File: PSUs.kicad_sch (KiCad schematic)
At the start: 33 parts, among them J19 Barrel_Jack, J20 AMP171826-4, Q1 DMP3013SFV-7, U16 AP64501SP-13

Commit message: removed HDMI, CAM and DISP1 connectors
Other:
- company: © 2020-2022 Raspberry Pi Ltd (formerly Raspberry Pi (Trading) Ltd.) -> (none)
- title: Compute Module 4 IO Board - PSUs -> Bitcart
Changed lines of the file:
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@@
   (paper "A4")
   (title_block
-    (title "Compute Module 4 IO Board - PSUs")
-    (company "© 2020-2022 Raspberry Pi Ltd (formerly Raspberry Pi (Trading) Ltd.)")
-    (comment 1 "www.raspberrypi.com")
+    (title "Bitcart")
+    (date "2023-09-15")
+    (rev "1")
   )
   (junction (at 76.2 130.302) (diameter 1.016) (color 0 0 0 0)

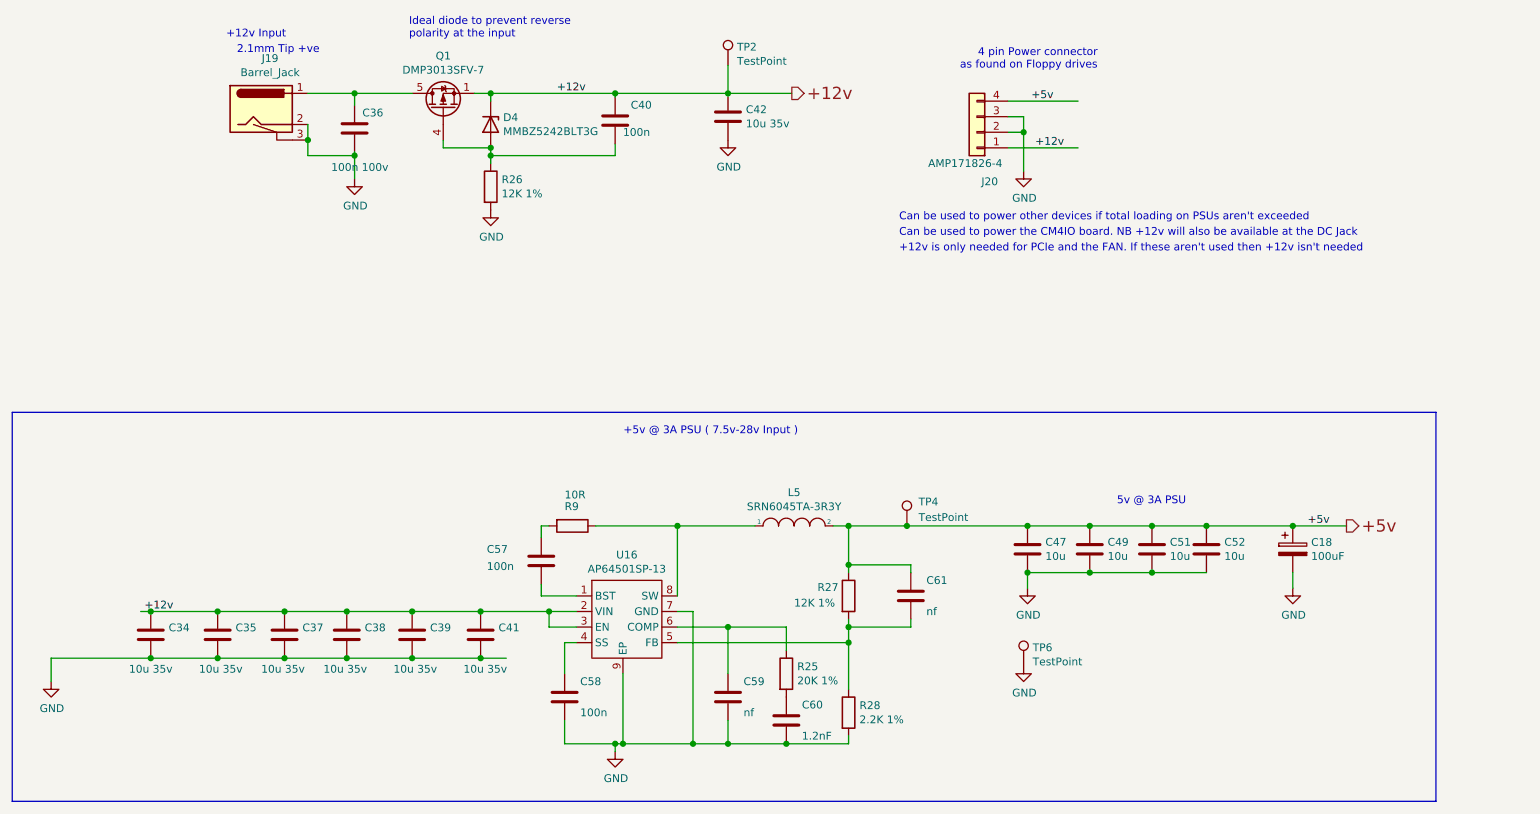
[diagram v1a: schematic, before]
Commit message: added hashboard connectors. added GPU power connector
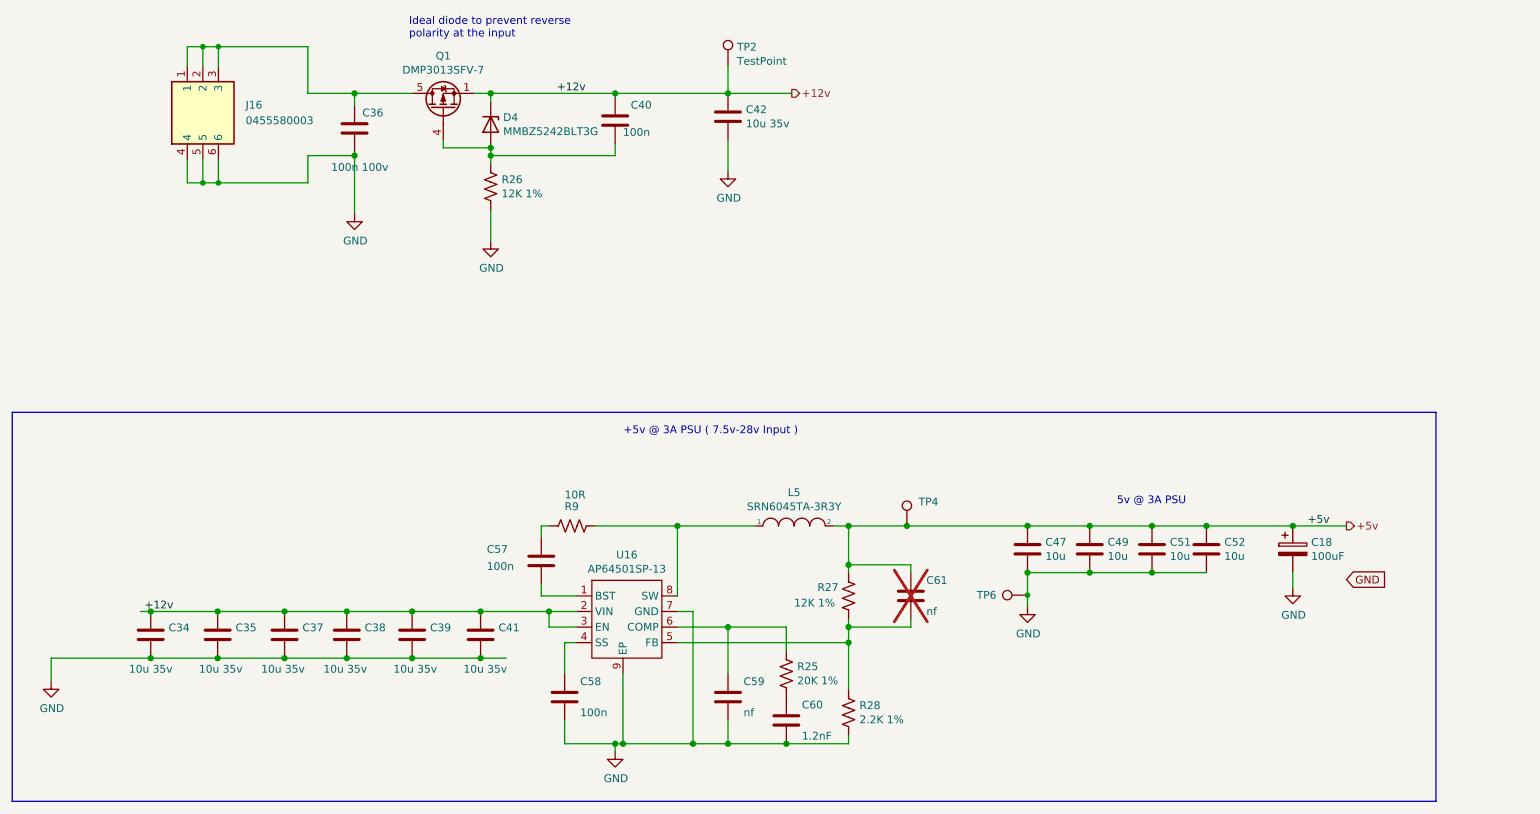
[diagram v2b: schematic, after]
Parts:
- removed J19: Barrel_Jack, CM4IO:BarrelJack_Horizontal, symbol CM4IO:Barrel_Jack
- removed J20: AMP171826-4, 171826-4:TE_171826-4, symbol Connector_Generic:Conn_01x04
- added J16: 0455580003, bitcart:0455580003, symbol bitcart:0455580003
- C61: now not fitted
- R25, R26, R27, R28, R9: symbol Device:R -> Device:R_US
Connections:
- net GND: now also J16.4, J16.5, J16.6
- net at C36.1, Q1.5 (D): now also J16.1, J16.2, J16.3
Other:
- note removed: "+12v Input"
- note removed: "+12v is only needed for PCIe and the FAN. If these aren't used then +12v isn't needed"
- note removed: "2.1mm Tip +ve"
- note removed: "4 pin Power connector as found on Floppy drives"
- note removed: "Can be used to power other devices if total loading on PSUs aren't exceeded"
- note removed: "Can be used to power the CM4IO board. NB +12v will also be available at the DC Jack"
- moved on the sheet: TP6

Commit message: extended the board to make room for IO connectors. added the vertical display connector.
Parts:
- TP2, TP4, TP6: footprint TestPoint:TestPoint_Pad_2.0x2.0mm -> TestPoint:TestPoint_Pad_D1.5mm
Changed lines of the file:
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@@
       (effects (font (size 1.27 1.27)) (justify left))
     )
-    (property "Footprint" "TestPoint:TestPoint_Pad_2.0x2.0mm" (at 153.67 41.148 0)
+    (property "Footprint" "TestPoint:TestPoint_Pad_D1.5mm" (at 153.67 41.148 0)
       (effects (font (size 1.27 1.27)) hide)
     )
@@
       (effects (font (size 1.27 1.27)) (justify left) hide)
     )
-    (property "Footprint" "TestPoint:TestPoint_Pad_2.0x2.0mm" (at 197.485 122.555 0)
+    (property "Footprint" "TestPoint:TestPoint_Pad_D1.5mm" (at 197.485 122.555 0)
       (effects (font (size 1.27 1.27)) hide)
     )
@@
       (effects (font (size 1.27 1.27)) (justify left) hide)
     )
-    (property "Footprint" "TestPoint:TestPoint_Pad_2.0x2.0mm" (at 182.88 116.332 0)
-      (effects (font (size 1.27 1.27)) hide)
-    )
+    (property "Footprint" "TestPoint:TestPoint_Pad_D1.5mm" (at 182.88 116.332 0)
+      (effects (font (size 1.27 1.27)) hide)
+    )

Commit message: added a lot more parts
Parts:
- C40, C57, C58: value 100n -> 0.1uF; DK (none) -> 478-KGM05AR71C104KHCT-ND; PARTNO (none) -> KGM05AR71C104KH; Part Description 0.1uF 10% 16V Ceramic Capacitor X7R 0402 (1005 Metric) -> (none)
- D4: DK (none) -> MMBZ5242BLT3GOSCT-ND; Field4 Digikey -> (none); Field5 MMBZ5242BLT3GOSCT-ND -> (none); Field6 MMBZ5242BLT3G -> (none); Field7 Onsemi -> (none); PARTNO (none) -> MMBZ5242BLT3G; Part Description Zener Diode 12V 225mW 5% Surface Mount SOT-23-3 (TO-236) -> (none)
- L5: DK (none) -> SRN6045TA-3R3YCT-ND; Field4 Farnell -> (none); Field5 2616889 -> (none); Field7 Bourns -> (none); Part Description 3.3µH Semi-Shielded Wirewound Inductor 7.8A 21mOhm Nonstand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 -> (none)
- Q1: DK (none) -> DMP3013SFV-7DICT-ND; Field4 Farnell -> (none); Field5 3405192 -> (none); Field6 DMP3013SFV-7 -> (none); Field7 Diodes -> (none); PARTNO (none) -> DMP3013SFV-7; Part Description DMP3013SFV-7 - Power MOSFET, P Channel, 30 V, 12 A, 0.008 o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 -> (none)
- U16: DK (none) -> 31-AP64501SP-13CT-ND; Field4 Digikey -> (none); Field5 31-AP64501SP-13CT-ND -> (none); Field6 AP64501SP-13 -> (none); Field7 Diodes -> (none); PARTNO (none) -> AP64501SP-13; Part Description Buck Switching Regulator IC Positive Adjustable 0.8V 1 Outp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 -> (none)
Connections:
- net +12v: now also D4.3 (K); no longer D4.1 (K)
- net at C40.2, Q1.4 (G), R26.1: now also D4.1 (A); no longer D4.2 (A)
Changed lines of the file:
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@@
       (effects (font (size 1.27 1.27)) hide)
     )
-    (property "Field4" "Digikey" (at 109.855 50.8 0)
-      (effects (font (size 1.27 1.27)) hide)
-    )
-    (property "Field5" "	MMBZ5242BLT3GOSCT-ND" (at 109.855 50.8 0)
-      (effects (font (size 1.27 1.27)) hide)
-    )
-    (property "Field6" "MMBZ5242BLT3G" (at 109.855 50.8 0)
-      (effects (font (size 1.27 1.27)) hide)
-    )
-    (property "Field7" "Onsemi" (at 109.855 50.8 0)
-      (effects (font (size 1.27 1.27)) hide)
-    )
-    (property "Part Description" "	Zener Diode 12V 225mW 5% Surface Mount SOT-23-3 (TO-236)" (at 109.855 50.8 0)
-      (effects (font (size 1.27 1.27)) hide)
-    )
-    (pin "1")
-    (pin "2")
+    (property "DK" "MMBZ5242BLT3GOSCT-ND" (at 109.855 50.8 0)
+      (effects (font (size 1.27 1.27)) hide)
+    )
+    (property "PARTNO" "MMBZ5242BLT3G" (at 109.855 50.8 0)
+      (effects (font (size 1.27 1.27)) hide)
+    )
+    (pin "1")
+    (pin "2")
+    (pin "3")
     (instances
       (project "bitcart"
@@
       (effects (font (size 1.27 1.27)) (justify left))
     )
-    (property "Value" "100n" (at 131.445 52.07 0)
+    (property "Value" "0.1uF" (at 131.445 52.07 0)
       (effects (font (size 1.27 1.27)) (justify left))
     )
@@
       (effects (font (size 1.27 1.27)) hide)
     )
-    (property "Part Description" "	0.1uF 10% 16V Ceramic Capacitor X7R 0402 (1005 Metric)" (at 130.175 50.165 0)
+    (property "Part Description" "" (at 130.175 50.165 0)
       (effects (font (size 1.27 1.27)) hide)
     )
@@
       (effects (font (size 1.27 1.27)) hide)
     )
+    (property "DK" "478-KGM05AR71C104KHCT-ND" (at 130.175 50.165 0)
+      (effects (font (size 1.27 1.27)) hide)
+    )
+    (property "PARTNO" "KGM05AR71C104KH" (at 130.175 50.165 0)
+      (effects (font (size 1.27 1.27)) hide)
+    )
     (pin "1")
     (pin "2")
@@
       (effects (font (size 1.27 1.27)) (justify left))
     )
-    (property "Value" "100n" (at 109.22 122.936 0)
+    (property "Value" "0.1uF" (at 109.22 122.936 0)
       (effects (font (size 1.27 1.27)) (justify left))
     )
@@
       (effects (font (size 1.27 1.27)) hide)
     )
-    (property "Part Description" "	0.1uF 10% 16V Ceramic Capacitor X7R 0402 (1005 Metric)" (at 118.11 122.047 0)
+    (property "Part Description" "" (at 118.11 122.047 0)
       (effects (font (size 1.27 1.27)) hide)
     )
     (property "Field8" "110091611" (at 118.11 122.047 0)
+      (effects (font (size 1.27 1.27)) hide)
+    )
+    (property "DK" "478-KGM05AR71C104KHCT-ND" (at 118.11 122.047 0)
+      (effects (font (size 1.27 1.27)) hide)
+    )
+    (property "PARTNO" "KGM05AR71C104KH" (at 118.11 122.047 0)
       (effects (font (size 1.27 1.27)) hide)
     )
@@
       (effects (font (size 1.27 1.27)) hide)
     )
-    (property "Field4" "Farnell" (at 159.385 116.332 0)
-      (effects (font (size 1.27 1.27)) hide)
-    )
-    (property "Field5" "2616889" (at 159.385 116.332 0)
+    (property "DK" "SRN6045TA-3R3YCT-ND" (at 159.385 116.332 0)
       (effects (font (size 1.27 1.27)) hide)
     )
@@
       (effects (font (size 1.27 1.27)) hide)
     )
-    (property "Field7" "Bourns" (at 159.385 116.332 0)
-      (effects (font (size 1.27 1.27)) hide)
-    )
-    (property "Part Description" "3.3µH Semi-Shielded Wirewound Inductor 7.8A 21mOhm Nonstandard" (at 159.385 116.332 0)
-      (effects (font (size 1.27 1.27)) hide)
-    )
     (pin "1")
     (pin "2")
@@
       (effects (font (size 1.27 1.27)) hide)
     )
-    (property "Field4" "Digikey" (at 131.445 130.302 0)
-      (effects (font (size 1.27 1.27)) hide)
-    )
-    (property "Field5" "31-AP64501SP-13CT-ND" (at 131.445 130.302 0)
-      (effects (font (size 1.27 1.27)) hide)
-    )
-    (property "Field6" "AP64501SP-13" (at 131.445 130.302 0)
-      (effects (font (size 1.27 1.27)) hide)
-    )
-    (property "Field7" "Diodes" (at 131.445 130.302 0)
-      (effects (font (size 1.27 1.27)) hide)
-    )
-    (property "Part Description" "Buck Switching Regulator IC Positive Adjustable 0.8V 1 Output 5A 8-SOIC (0.154\", 3.90mm Width) Exposed Pad" (at 131.445 130.302 0)
+    (property "DK" "31-AP64501SP-13CT-ND" (at 131.445 130.302 0)
+      (effects (font (size 1.27 1.27)) hide)
+    )
+    (property "PARTNO" "AP64501SP-13" (at 131.445 130.302 0)
       (effects (font (size 1.27 1.27)) hide)
     )
@@
       (effects (font (size 1.27 1.27)) (justify left))
     )
-    (property "Value" "100n" (at 124.46 146.812 0)
+    (property "Value" "0.1uF" (at 124.46 146.812 0)
       (effects (font (size 1.27 1.27)) (justify left))
     )
@@
       (effects (font (size 1.27 1.27)) hide)
     )
-    (property "Part Description" "	0.1uF 10% 16V Ceramic Capacitor X7R 0402 (1005 Metric)" (at 121.92 144.272 0)
+    (property "Part Description" "" (at 121.92 144.272 0)
       (effects (font (size 1.27 1.27)) hide)
     )
     (property "Field8" "110091611" (at 121.92 144.272 0)
+      (effects (font (size 1.27 1.27)) hide)
+    )
+    (property "DK" "478-KGM05AR71C104KHCT-ND" (at 121.92 144.272 0)
+      (effects (font (size 1.27 1.27)) hide)
+    )
+    (property "PARTNO" "KGM05AR71C104KH" (at 121.92 144.272 0)
       (effects (font (size 1.27 1.27)) hide)
     )
@@
       (effects (font (size 1.27 1.27)) (justify left) hide)
     )
-    (property "Field4" "Farnell" (at 102.108 48.26 0)
-      (effects (font (size 1.27 1.27)) hide)
-    )
-    (property "Field5" "3405192" (at 102.108 48.26 0)
-      (effects (font (size 1.27 1.27)) hide)
-    )
-    (property "Field6" "DMP3013SFV-7" (at 102.108 48.26 0)
-      (effects (font (size 1.27 1.27)) hide)
-    )
-    (property "Field7" "Diodes" (at 102.108 48.26 0)
-      (effects (font (size 1.27 1.27)) hide)
-    )
-    (property "Part Description" "DMP3013SFV-7 -  Power MOSFET, P Channel, 30 V, 12 A, 0.008 ohm, PowerDI3333, Surface Mount" (at 102.108 48.26 0)
-      (effects (font (size 1.27 1.27)) hide)
-    )
+    (property "DK" "DMP3013SFV-7DICT-ND" (at 102.108 48.26 90)
+      (effects (font (size 1.27 1.27)) hide)
+    )
+    (property "PARTNO" "DMP3013SFV-7" (at 102.108 48.26 90)
+      (effects (font (size 1.27 1.27)) hide)
+    )

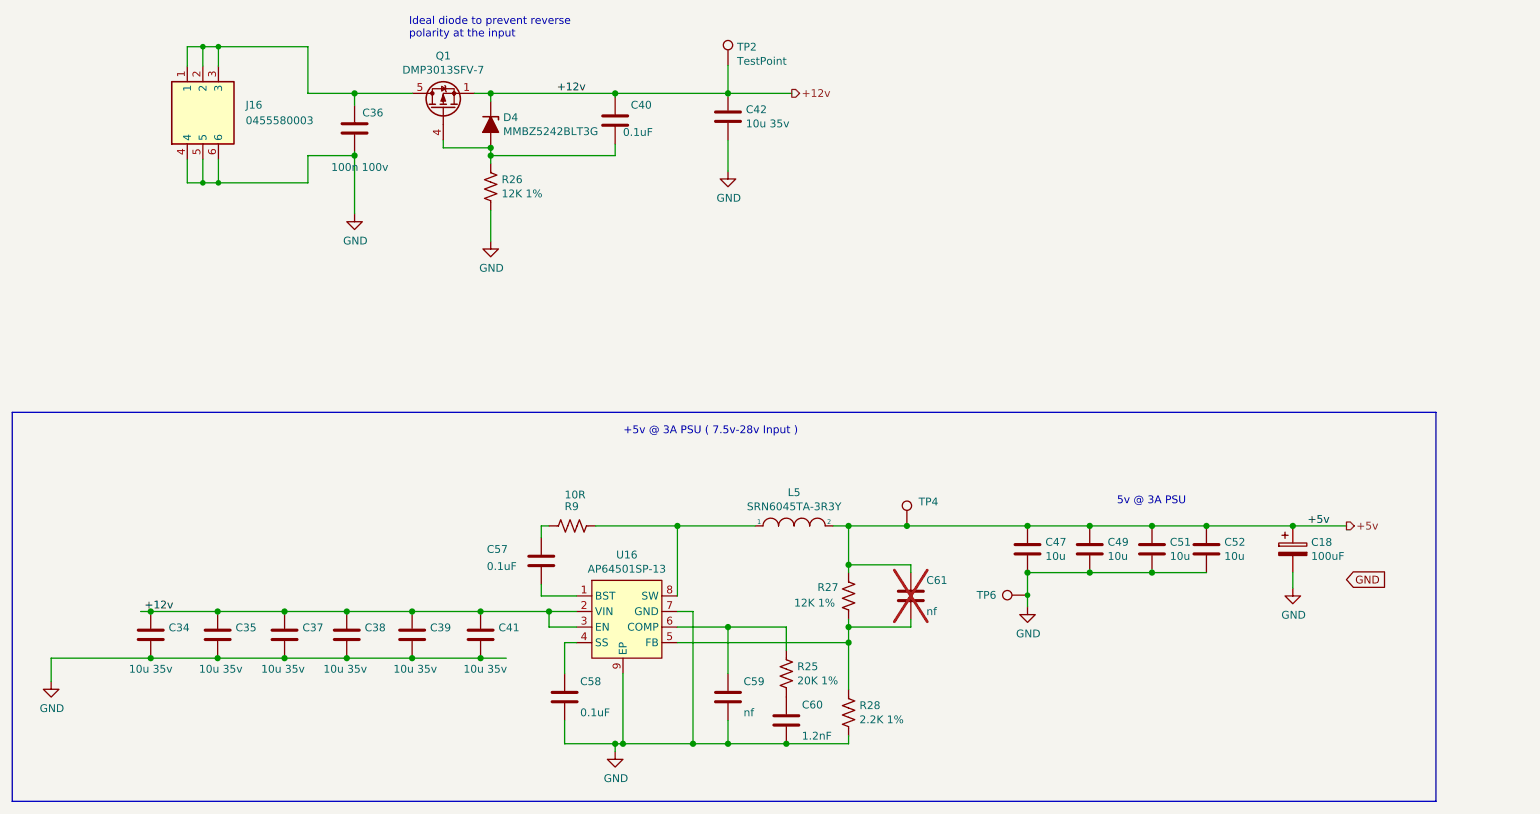
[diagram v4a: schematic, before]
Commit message: resolved some schematic-board errors. switched to tap-on-top ethernet.
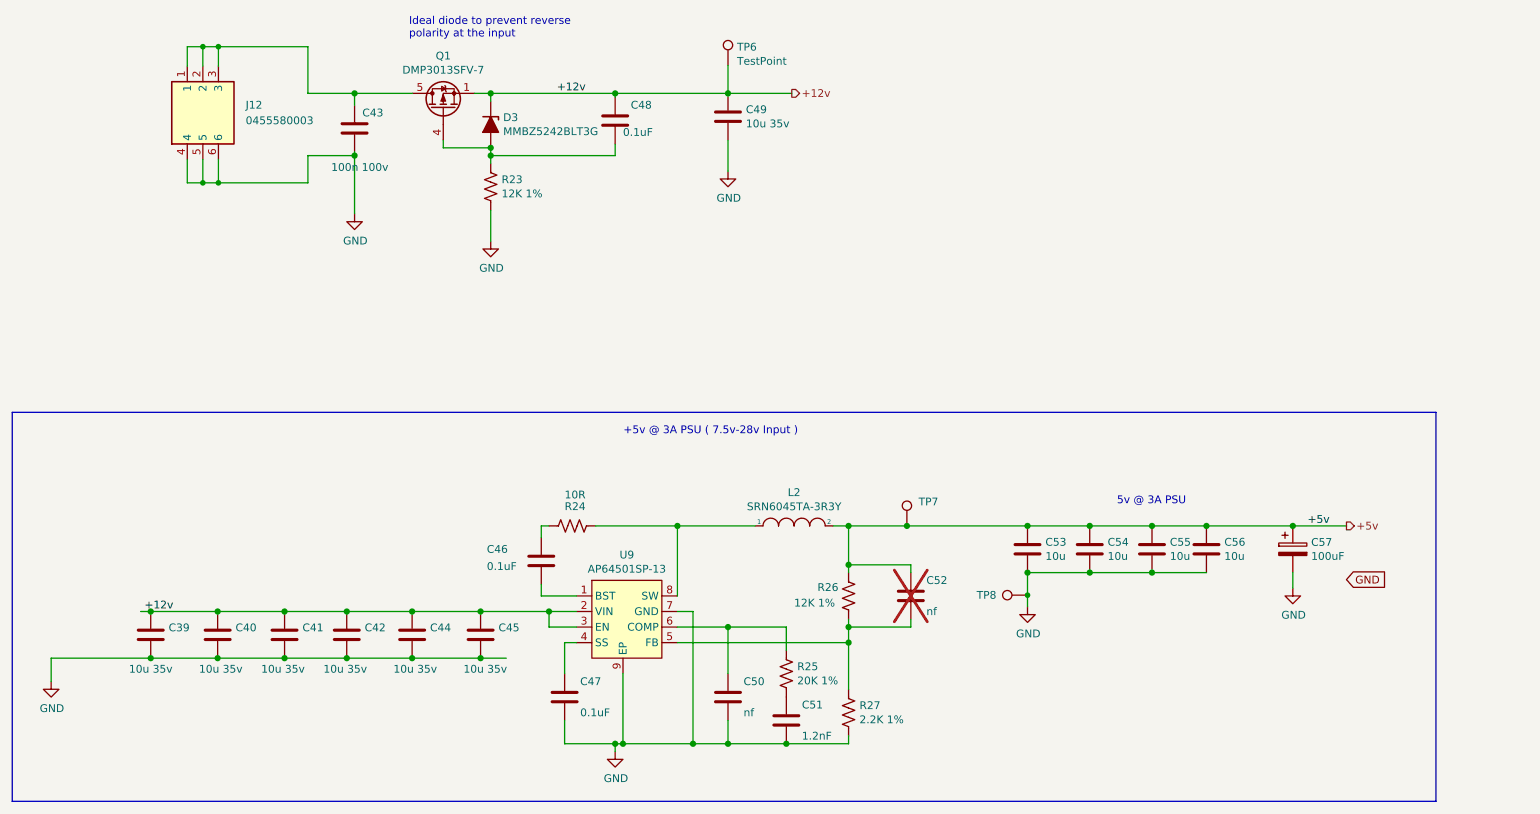
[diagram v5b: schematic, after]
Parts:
- D3: renamed from D4; footprint Diode_SMD:D_SOT-23_ANK -> bitcart:D_SOT-23_ANK
- renumbered C34 to C39, C35 to C40, C37 to C41, C38 to C42, C36 to C43, C39 to C44, C41 to C45, C57 to C46, C58 to C47, C40 to C48, C42 to C49, C59 to C50, C60 to C51, C61 to C52, C47 to C53, C49 to C54, C51 to C55, C52 to C56, C18 to C57, J16 to J12, L5 to L2, R26 to R23, R9 to R24, R27 to R26, R28 to R27, TP2 to TP6, TP4 to TP7, TP6 to TP8, U16 to U9
